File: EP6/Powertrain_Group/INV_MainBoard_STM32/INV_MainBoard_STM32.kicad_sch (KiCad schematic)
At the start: 15 parts, among them J1 FX26-30P-1SV, J10 current_DC, J2 motorSense, J9 CAN

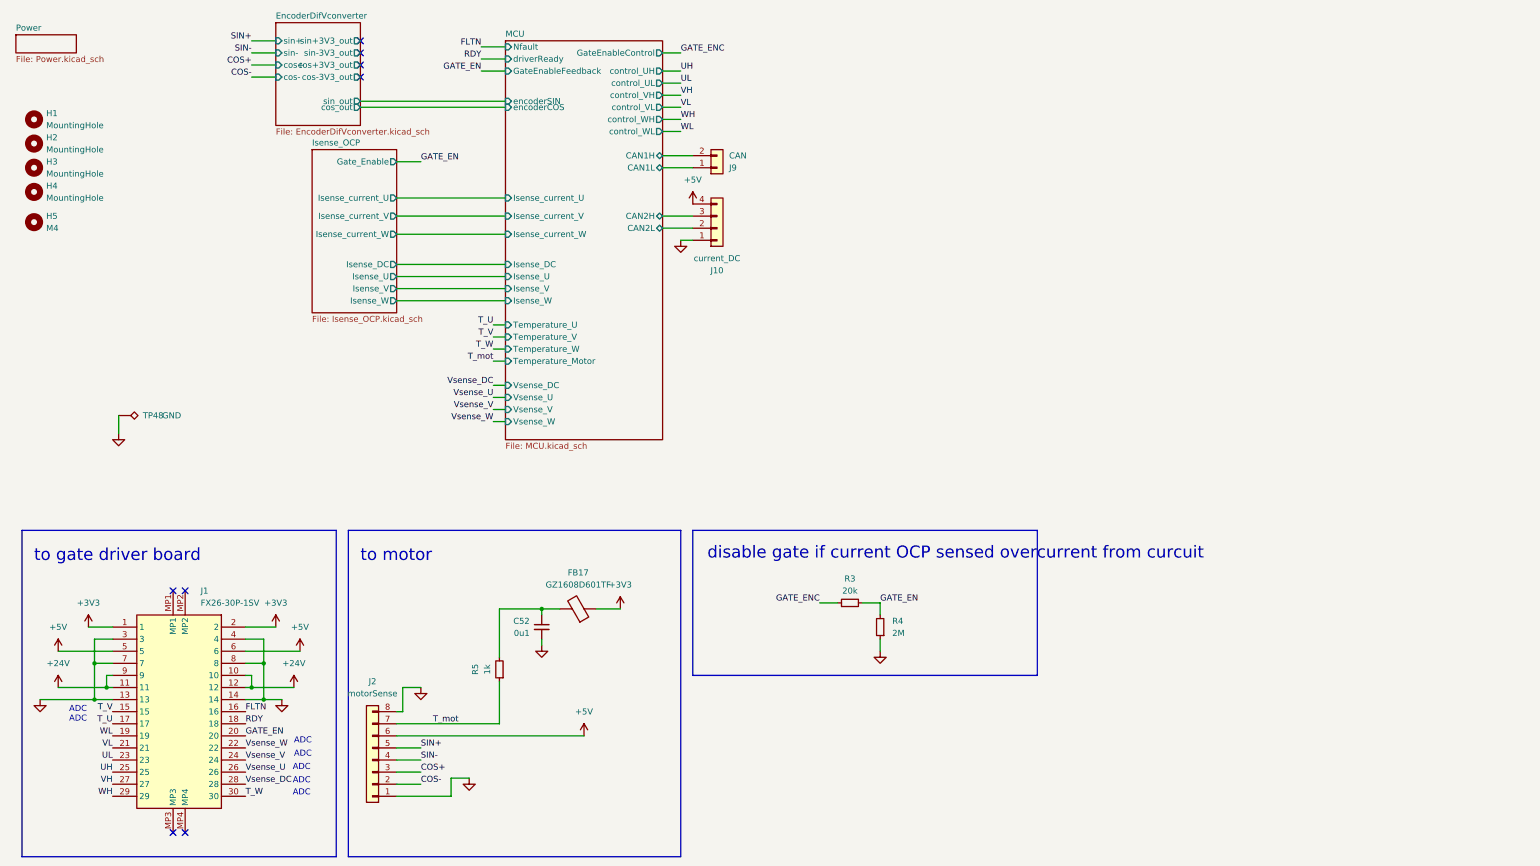
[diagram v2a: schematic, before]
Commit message: update INV_MainBoard_STM32 to V2.0
big update to match new INV_GateDriver
and use H743ZI as MCU
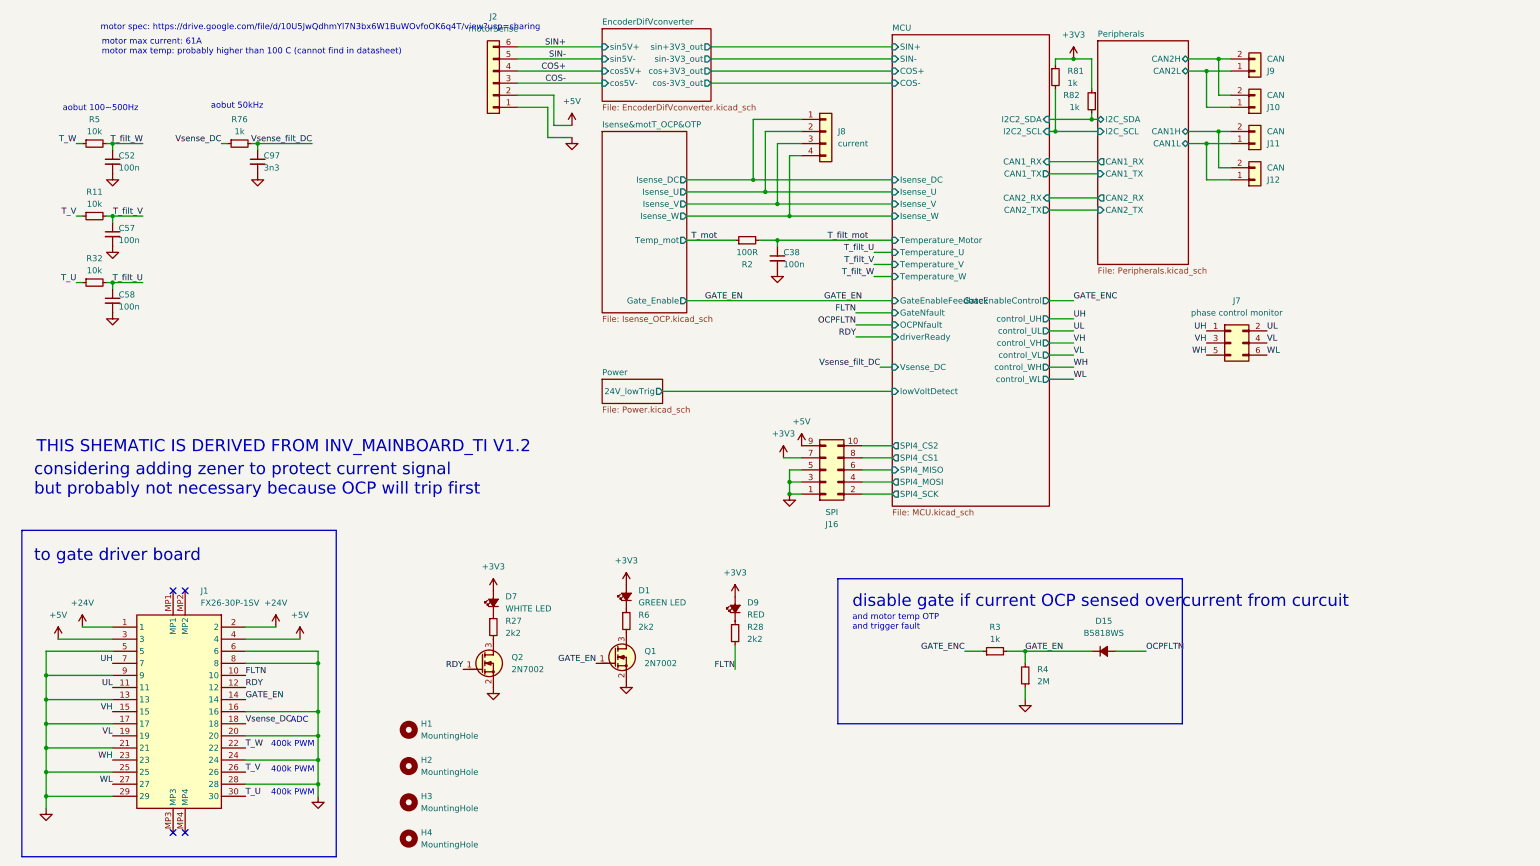
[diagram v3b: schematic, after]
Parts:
- removed FB17: GZ1608D601TF, Inductor_SMD:L_0805_2012Metric, symbol Device:FerriteBead
- removed H5: M4, MountingHole:MountingHole_4mm, symbol Mechanical:MountingHole
- removed J10: current_DC, Connector_JST:JST_XH_B4B-XH-A_1x04_P2.50mm_Vertical, symbol PCM_4ms_Connector:Conn_01x04
- removed TP48: GND, TestPoint:TestPoint_THTPad_D1.0mm_Drill0.5mm, symbol Connector:TestPoint_Alt
- added C38, C57, C58: 100n, Capacitor_SMD:C_0402_1005Metric, symbol Device:C_Small
- added C97: 3n3, Capacitor_SMD:C_0402_1005Metric, symbol Device:C_Small
- added D1: GREEN LED, LED_SMD:LED_0805_2012Metric, symbol Device:LED_Small_Filled
- added D15: B5818WS, Diode_SMD:D_SOD-323, symbol Device:D_Small_Filled
- added D7: WHITE LED, LED_SMD:LED_0805_2012Metric, symbol Device:LED_Small_Filled
- added D9: RED, LED_SMD:LED_0805_2012Metric, symbol Device:LED_Small_Filled
- added J10, J11, J12: CAN, Connector_JST:JST_XH_B2B-XH-A_1x02_P2.50mm_Vertical, symbol Connector_Generic:Conn_01x02
- added J16: SPI, Connector_PinHeader_2.54mm:PinHeader_2x05_P2.54mm_Vertical, symbol Connector_Generic:Conn_02x05_Odd_Even
- added J7: phase control monitor, Connector_PinHeader_2.54mm:PinHeader_2x03_P2.54mm_Vertical, symbol Connector_Generic:Conn_02x03_Odd_Even
- added J8: current, Connector_PinHeader_2.54mm:PinHeader_1x04_P2.54mm_Vertical, symbol Connector_Generic:Conn_01x04
- added Q1, Q2: 2N7002, Package_TO_SOT_SMD:SOT-23, symbol PCM_Transistor_MOSFET_AKL:2N7002
- added R11, R32: 10k, Resistor_SMD:R_0402_1005Metric, symbol Device:R_Small
- added R2: 100R, Resistor_SMD:R_0402_1005Metric, symbol Device:R_Small
- added R27, R28, R6: 2k2, Resistor_SMD:R_0402_1005Metric, symbol Device:R_Small
- added R76, R81, R82: 1k, Resistor_SMD:R_0402_1005Metric, symbol Device:R_Small
- C52: value 0u1 -> 100n
- H1, H2, H3, H4: now in the parts list
- J2: footprint Connector_JST:JST_XH_B8B-XH-A_1x08_P2.50mm_Vertical -> Connector_JST:JST_XH_B6B-XH-A_1x06_P2.50mm_Vertical; symbol PCM_4ms_Connector:Conn_01x08 -> Connector_Generic:Conn_01x06
- R3: value 20k -> 1k
- R5: value 1k -> 10k; footprint Resistor_SMD:R_0603_1608Metric -> Resistor_SMD:R_0402_1005Metric
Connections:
- net Vsense_U is gone; now on net T_V: J1.26
- net Vsense_V is gone; now on net GND: J1.24
- net Vsense_W is gone; now on net T_W: J1.22
- net +24V: now also J1.1, J1.2; no longer J1.10, J1.11, J1.12, J1.9
- net +3V3: now also D1.2 (A), D7.2 (A), D9.2 (A), J16.7 (Pin_7), R81.1, R82.1; no longer J1.1, J1.2
- net +5V: now also J1.3, J1.4, J2.2 (Pin_2), J16.9 (Pin_9); no longer J1.5, J1.6, J2.6 (Pin_6)
- net COS+: now also J2.4 (Pin_4); no longer J2.3 (Pin_3)
- net COS-: now also J2.3 (Pin_3); no longer J2.2 (Pin_2)
- net FLTN: now also J1.10, R28.2; no longer J1.16
- net GATE_EN: now also J1.14, D15.1 (K), Q1.1 (G); no longer J1.20
- net GND: now also J1.16, J1.17, J1.20, J1.21, J1.25, J1.28, J1.29, J1.5, J1.6, J1.9, C38.2, C57.2, C58.2, C97.2, J16.1 (Pin_1), J16.3 (Pin_3), J16.5 (Pin_5), Q1.2 (S), Q2.2 (S); no longer J1.14, J1.3, J1.4, J1.7, J2.8 (Pin_8)
- net Isense&motT_OCP&OTP/Isense_DC: now also J8.1 (Pin_1)
- net Isense&motT_OCP&OTP/Isense_U: now also J8.2 (Pin_2)
- net Isense&motT_OCP&OTP/Isense_V: now also J8.3 (Pin_3)
- net Isense&motT_OCP&OTP/Isense_W: now also J8.4 (Pin_4)
- net RDY: now also J1.12, Q2.1 (G); no longer J1.18
- net SIN+: now also J2.6 (Pin_6); no longer J2.5 (Pin_5)
- net SIN-: now also J2.5 (Pin_5); no longer J2.4 (Pin_4)
- net T_U: now also J1.30, R32.1; no longer J1.17
- net T_V: now also R11.1; no longer J1.15
- net T_W: now also R5.1; no longer J1.30
- net T_mot: now also R2.1; no longer J2.7 (Pin_7), R5.1
- net UH: now also J1.7, J7.1 (Pin_1); no longer J1.25
- net UL: now also J1.11, J7.2 (Pin_2); no longer J1.23
- net VH: now also J1.15, J7.3 (Pin_3); no longer J1.27
- net VL: now also J1.19, J7.4 (Pin_4); no longer J1.21
- net Vsense_DC: now also J1.18, R76.1; no longer J1.28
- net WH: now also J1.23, J7.5 (Pin_5); no longer J1.29
- net WL: now also J1.27, J7.6 (Pin_6); no longer J1.19
- net T_filt_W: now reaches C52.1, R5.2
- net MCU/CAN1H renamed Peripherals/CAN2H
- net Peripherals/CAN2H: now also J10.2 (Pin_2)
- net MCU/CAN1L renamed Peripherals/CAN2L
- net Peripherals/CAN2L: now also J10.1 (Pin_1)
- new net: D9.1 (K), R28.1
- new net: D7.1 (K), R27.1
- new net: Q2.3 (D), R27.2
- new net: D1.1 (K), R6.1
- new net: Q1.3 (D), R6.2
- new net MCU/I2C2_SCL: R81.2
- new net MCU/I2C2_SDA: R82.2
- new net MCU/SPI4_CS1: J16.8 (Pin_8)
- new net MCU/SPI4_CS2: J16.10 (Pin_10)
- new net MCU/SPI4_MISO: J16.6 (Pin_6)
- new net MCU/SPI4_MOSI: J16.4 (Pin_4)
- new net MCU/SPI4_SCK: J16.2 (Pin_2)
- new net OCPFLTN: D15.2 (A)
- new net Peripherals/CAN1H: J11.2 (Pin_2), J12.2 (Pin_2)
- new net Peripherals/CAN1L: J11.1 (Pin_1), J12.1 (Pin_1)
- new net T_filt_U: C58.1, R32.2
- new net T_filt_V: C57.1, R11.2
- new net T_filt_mot: C38.1, R2.2
- new net Vsense_filt_DC: C97.1, R76.2
- no-connect marks 8 -> 4
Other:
- sheet Isense_OCP renamed Isense&motT_OCP&OTP
- added sheet Peripherals (Peripherals.kicad_sch)
- sheet EncoderDifVconverter ports: added cos5V+, cos5V-, sin5V+, sin5V-; removed cos+, cos-, cos_out, sin+, sin-, sin_out
- sheet Isense&motT_OCP&OTP ports: added Temp_mot; removed Isense_current_U, Isense_current_V, Isense_current_W
- sheet MCU ports: added CAN1_RX, CAN1_TX, CAN2_RX, CAN2_TX, COS+, COS-, GateNfault, I2C2_SCL, I2C2_SDA, OCPNfault, SIN+, SIN-, SPI4_CS1, SPI4_CS2, SPI4_MISO, SPI4_MOSI, SPI4_SCK, lowVoltDetect; removed CAN1H, CAN1L, CAN2H, CAN2L, Isense_current_U, Isense_current_V, Isense_current_W, Nfault, Vsense_U, Vsense_V, Vsense_W, encoderCOS, encoderSIN
- sheet Power ports: added 24V_lowTrig; removed none
- note added: "400k PWM"
- note added: "THIS SHEMATIC IS DERIVED FROM INV_MAINBOARD_TI V1.2"
- note added: "and motor temp OTP"
- note added: "and trigger fault"
- note added: "aobut 100~500Hz"
- note added: "aobut 50kHz"
- note added: "considering adding zener to protect current signal but probably not necessary because OCP will trip first"
- note added: "motor max current: 61A motor max temp: probably higher than 100 C (cannot find in datasheet)"
- note added: "motor spec: https://drive.google.com/file/d/10U5JwQdhmYl7N3bx6W1BuWOvfoOK6q4T/view?usp=sharing"
- note removed: "to motor"
- title: INV_MainBoard -> INV_MainBoard_STM32
- moved on the sheet: J9, R3, R4

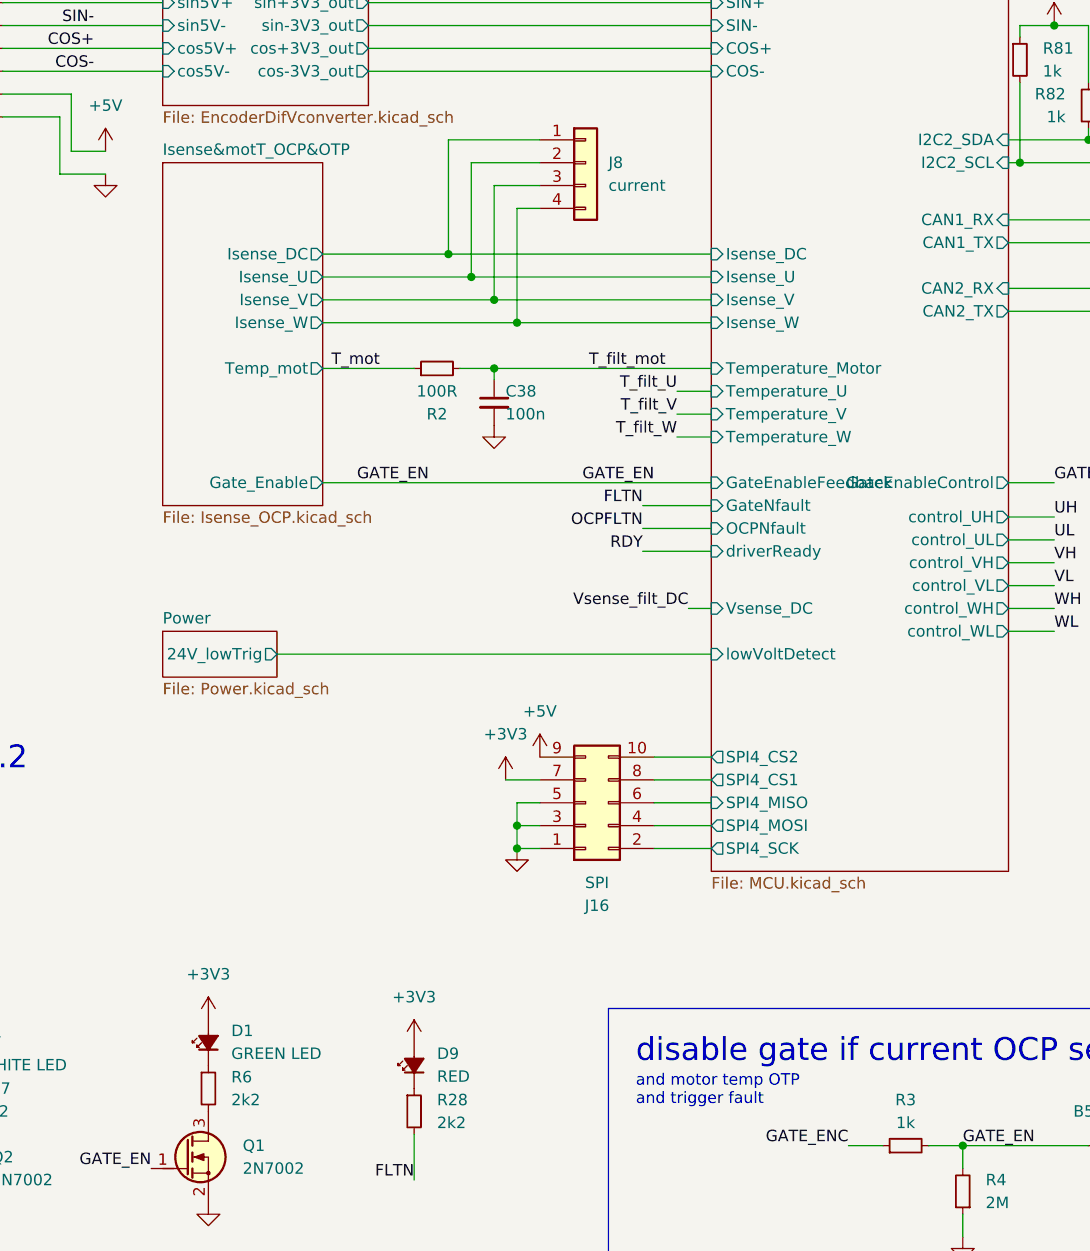
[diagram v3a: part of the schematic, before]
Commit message: update INV_MainBoard_STM32 to V2.1
update for JLCPCB, include change in 1.65 Vref and some name change for easier JLCPCBA BOM selection
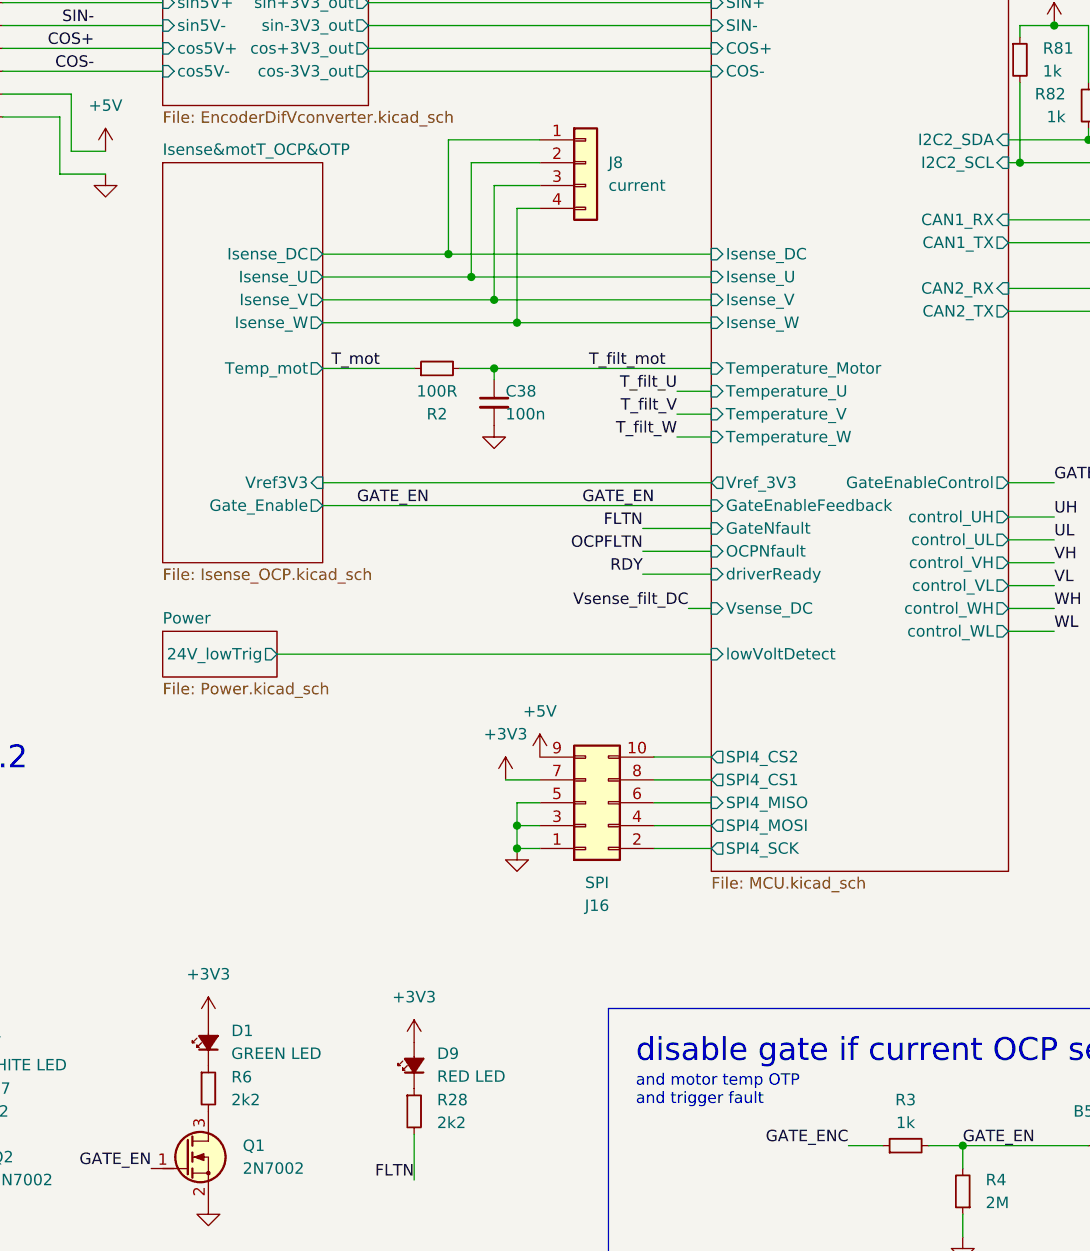
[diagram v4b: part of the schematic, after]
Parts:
- D9: value RED -> RED LED
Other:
- sheet Isense&motT_OCP&OTP ports: added Vref3V3; removed none
- sheet MCU ports: added Vref_3V3; removed none
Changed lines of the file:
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@@
 	(title_block
 		(title "INV_MainBoard_STM32")
-		(rev "2.0")
+		(date "2025-02-28")
+		(rev "2.1")
 		(company "NTURacing Team")
 		(comment 1 "郭哲明 Jack Kuo")
@@
 	(wire
 		(pts
-			(xy 156.21 73.66) (xy 199.39 73.66)
+			(xy 156.21 76.2) (xy 199.39 76.2)
 		)
 		(stroke
@@
 	(wire
 		(pts
+			(xy 156.21 73.66) (xy 199.39 73.66)
+		)
+		(stroke
+			(width 0)
+			(type default)
+		)
+	)
+	(wire
+		(pts
 			(xy 21.59 147.32) (xy 21.59 152.4)
 		)
@@
 	(wire
 		(pts
-			(xy 191.77 81.28) (xy 199.39 81.28)
+			(xy 191.77 83.82) (xy 199.39 83.82)
 		)
 		(stroke
@@
 	(wire
 		(pts
-			(xy 191.77 76.2) (xy 199.39 76.2)
+			(xy 191.77 78.74) (xy 199.39 78.74)
 		)
 		(stroke
@@
 	(wire
 		(pts
-			(xy 191.77 78.74) (xy 199.39 78.74)
+			(xy 191.77 81.28) (xy 199.39 81.28)
 		)
 		(stroke
@@
 	)
 	(label "FLTN"
-		(at 191.77 76.2 180)
+		(at 191.77 78.74 180)
 		(effects
 			(font
@@
 	)
 	(label "GATE_EN"
-		(at 160.02 73.66 0)
+		(at 160.02 76.2 0)
 		(effects
 			(font
@@
 	)
 	(label "OCPFLTN"
-		(at 191.77 78.74 180)
+		(at 191.77 81.28 180)
 		(effects
 			(font
@@
 	)
 	(label "RDY"
-		(at 191.77 81.28 180)
+		(at 191.77 83.82 180)
 		(effects
 			(font
@@
 	)
 	(label "GATE_EN"
-		(at 193.04 73.66 180)
+		(at 193.04 76.2 180)
 		(effects
 			(font
@@
 			)
 		)
-		(property "Value" "RED"
+		(property "Value" "RED LED"
 			(at 168.91 139.6365 90)
 			(effects
@@
 	(sheet
 		(at 138.43 38.1)
-		(size 17.78 38.1)
+		(size 17.78 44.45)
 		(fields_autoplaced yes)
 		(stroke
@@
 		)
 		(property "Sheetfile" "Isense_OCP.kicad_sch"
-			(at 138.43 76.7846 0)
+			(at 138.43 83.1346 0)
 			(effects
 				(font
@@
 		)
 		(pin "Gate_Enable" output
-			(at 156.21 73.66 0)
+			(at 156.21 76.2 0)
 			(effects
 				(font
@@
 			)
 		)
+		(pin "Vref3V3" input
+			(at 156.21 73.66 0)
+			(effects
+				(font
+					(size 1.27 1.27)
+				)
+				(justify right)
+			)
+		)
 		(instances
 			(project "INV_MainBoard_STM32"
@@
 		)
 		(pin "driverReady" input
-			(at 199.39 81.28 180)
+			(at 199.39 83.82 180)
 			(effects
 				(font
@@
 		)
 		(pin "GateEnableFeedback" input
-			(at 199.39 73.66 180)
+			(at 199.39 76.2 180)
 			(effects
 				(font
@@
 		)
 		(pin "GateNfault" input
-			(at 199.39 76.2 180)
+			(at 199.39 78.74 180)
 			(effects
 				(font
@@
 		)
 		(pin "OCPNfault" input
-			(at 199.39 78.74 180)
+			(at 199.39 81.28 180)
 			(effects
 				(font
@@
 			(effects
 				(font
+					(size 1.27 1.27)
+				)
+				(justify left)
+			)
+		)
+		(pin "Vref_3V3" output
+			(at 199.39 73.66 180)
+			(effects
+				(font
